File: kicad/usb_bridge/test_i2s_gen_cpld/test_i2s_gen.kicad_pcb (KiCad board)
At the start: 2 copper layers, 40 x 40 mm, 81 parts, among them J1 Conn_01x02_Male, J2 Conn_02x05_Odd_Even, J3 Conn_01x02_Male, U1 SIT2001B, U2 AMS1117-3.3, U3 AMS1117-1.8, U4 5M40ZE64C5N

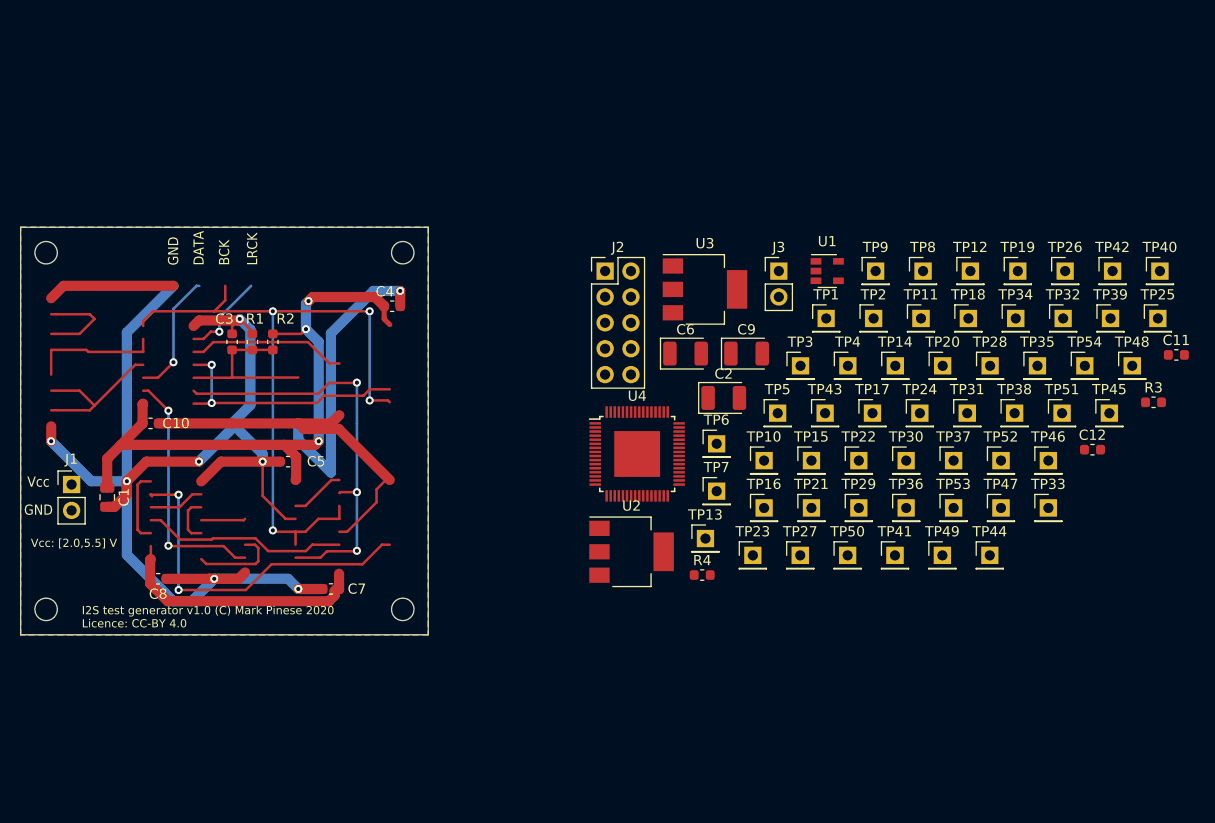
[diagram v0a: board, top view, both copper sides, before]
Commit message: I2S test generator refinements
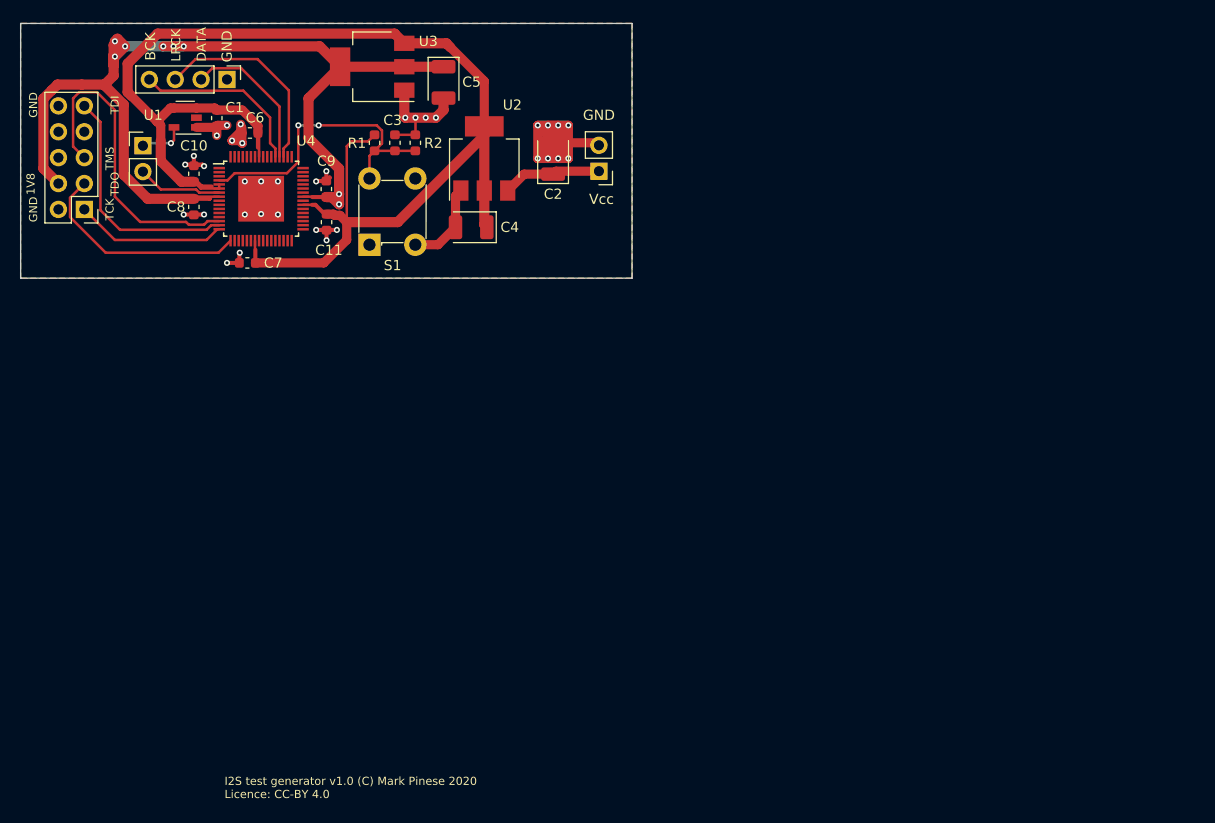
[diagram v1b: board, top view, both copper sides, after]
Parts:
- removed the C4 at (166.5, 87.8)
- removed the C5 at (156.2, 103.0)
- removed the C8 at (143.5, 114.5)
- removed H1, H2, H3, H4: MountingHole, MountingHole:MountingHole_2.2mm_M2
- removed R3, R4: R, Resistor_SMD:R_0603_1608Metric
- removed TP1, TP10, TP11, TP12, TP13, TP14, TP15, TP16, TP17, TP18, TP19, TP2, TP20, TP21, TP22, TP23, TP24, TP25, TP26, TP27, TP28, TP29, TP3, TP30, TP31, TP32, TP33, TP34, TP35, TP36, TP37, TP38, TP39, TP4, TP40, TP41, TP42, TP43, TP44, TP45, TP46, TP47, TP48, TP49, TP5, TP50, TP51, TP52, TP53, TP54, TP6, TP7, TP8, TP9: ~, Connector_PinHeader_2.54mm:PinHeader_1x01_P2.54mm_Vertical
- added C11: 100n, Capacitor_SMD:C_0603_1608Metric, F.Cu at (160.0, 79.5)
- added C6: 100n, Capacitor_SMD:C_0603_1608Metric, F.Cu at (152.5, 70.8)
- added J4: Conn_01x04_Male, Connector_PinHeader_2.54mm:PinHeader_1x04_P2.54mm_Vertical, F.Cu at (150.2, 65.5)
- added S1: 1825910-6, project_footprints:Switch_Tactile_THT_6x6mm, F.Cu at (164.2, 81.7)
- C1: value 10u -> 100n; footprint Capacitor_SMD:C_0805_2012Metric -> Capacitor_SMD:C_0603_1608Metric
- moved C8 97.5 mm to (147.0, 78.0), turned to 270 degrees
- moved C9 79.4 mm to (160.0, 76.2), turned to 90 degrees
- moved U1 64.8 mm to (146.2, 69.2), turned to 180 degrees
- moved J3 63.6 mm to (142.0, 72.0)
- moved J1 60.2 mm to (186.8, 74.5), turned to 180 degrees
- moved J2 51.5 mm to (136.2, 78.2), turned to 180 degrees
- moved U4 44.6 mm to (153.6, 77.2)
- moved U2 41.2 mm to (175.5, 73.2), turned to 90 degrees
- moved C5 39.9 mm to (171.5, 65.8), turned to 270 degrees
- moved U3 39.3 mm to (164.5, 64.2), turned to 180 degrees
- moved C1 38.7 mm to (149.2, 69.3)
- moved C7 33.0 mm to (152.2, 83.5)
- moved C2 28.9 mm to (182.2, 73.2), turned to 90 degrees
- moved C3 25.2 mm to (166.7, 71.7)
- moved R2 25.2 mm to (168.7, 71.7)
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- renumbered C6 to C4, C9 to C5, C11 to C8, C12 to C9
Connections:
- net Net-(C2-Pad1) renamed /Vcc
- C3 pad 1: Net-(C3-Pad1) -> /~RESET
- J2 pad 4: Net-(J2-Pad4) -> +1V8
- J3 pad 2: /CLK2 -> /CLK12
- R1 pad 1: Net-(C3-Pad1) -> /~RESET
- R2 pad 2: Net-(C3-Pad1) -> /~RESET
- U1 pad 5: /CLK2 -> Net-(J3-Pad1)
- U4 pad 4: Net-(TP17-Pad1) -> /~RESET
- U4 pad 5: Net-(TP3-Pad1) -> +3V3
- U4 pad 51: Net-(TP34-Pad1) -> /LRCK
- U4 pad 52: Net-(TP49-Pad1) -> /DATA
- U4 pad 53: Net-(TP35-Pad1) -> /BCK
- U4 pad 7: Net-(TP4-Pad1) -> /CLK12
- U4 pad 9: Net-(J3-Pad1) -> Net-(U4-Pad9)
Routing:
- net GNDD: track 206.9 -> 87.1 mm, vias 8 -> 35
- net +1V8: track 0.00 -> 109.9 mm, vias 0 -> 8
- net +3V3: track 86.3 -> 137.4 mm, vias 3 -> 0
- net /BCK: track 68.0 -> 17.5 mm, vias 4 -> 0
- net /~Reset: track 41.2 -> 0.00 mm, vias 3 -> 0
- net Net-(U2-Pad9): track 34.9 -> 0.00 mm, vias 2 -> 0
- net /TMS: track 0.00 -> 31.4 mm
- net /~RESET: track 0.00 -> 29.7 mm, vias 0 -> 2
- net /Reset: track 25.4 -> 0.00 mm, vias 2 -> 0
- net Net-(U1-Pad13): track 24.5 -> 0.00 mm, vias 2 -> 0
- net /TDI: track 0.00 -> 23.5 mm
- net /TDO: track 0.00 -> 21.6 mm
- net Net-(U2-Pad11): track 20.1 -> 0.00 mm
- net Net-(C3-Pad1): track 17.0 -> 0.00 mm
- net Net-(U1-Pad5): track 15.6 -> 0.00 mm
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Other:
- board size 40 x 40 mm -> 60 x 25 mm
- net class Default: clearance 0.2 -> 0.127; via_dia 0.8 -> 0.6; via_drill 0.4 -> 0.3
- rule trace_clearance: 0.2 -> 0.127
- rule trace_min: 0.2 -> 0.127
- rule via_min_drill: 0.3 -> 0.2
- rule via_min_size: 0.4 -> 0.45
- board text added: "1V8"
- board text added: "TCK"
- board text added: "TDI"
- board text added: "TDO"
- board text added: "TMS"
- board text removed: "Vcc: [2.0,5.5] V"
